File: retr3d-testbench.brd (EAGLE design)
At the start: 101.9 x 53.3 mm, 72 parts, among them U1 ARDUINO-MEGAFULL

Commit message: Update
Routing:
- net N$1: track 18.6 -> 20.7 mm
- net N$38: track 21.6 -> 23.1 mm
- net N$30: track 18.6 -> 19.5 mm
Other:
- board text added: "For assembly and usage goto"
- board text added: "Github.com/masterperson40/Retr3d-Testbench"

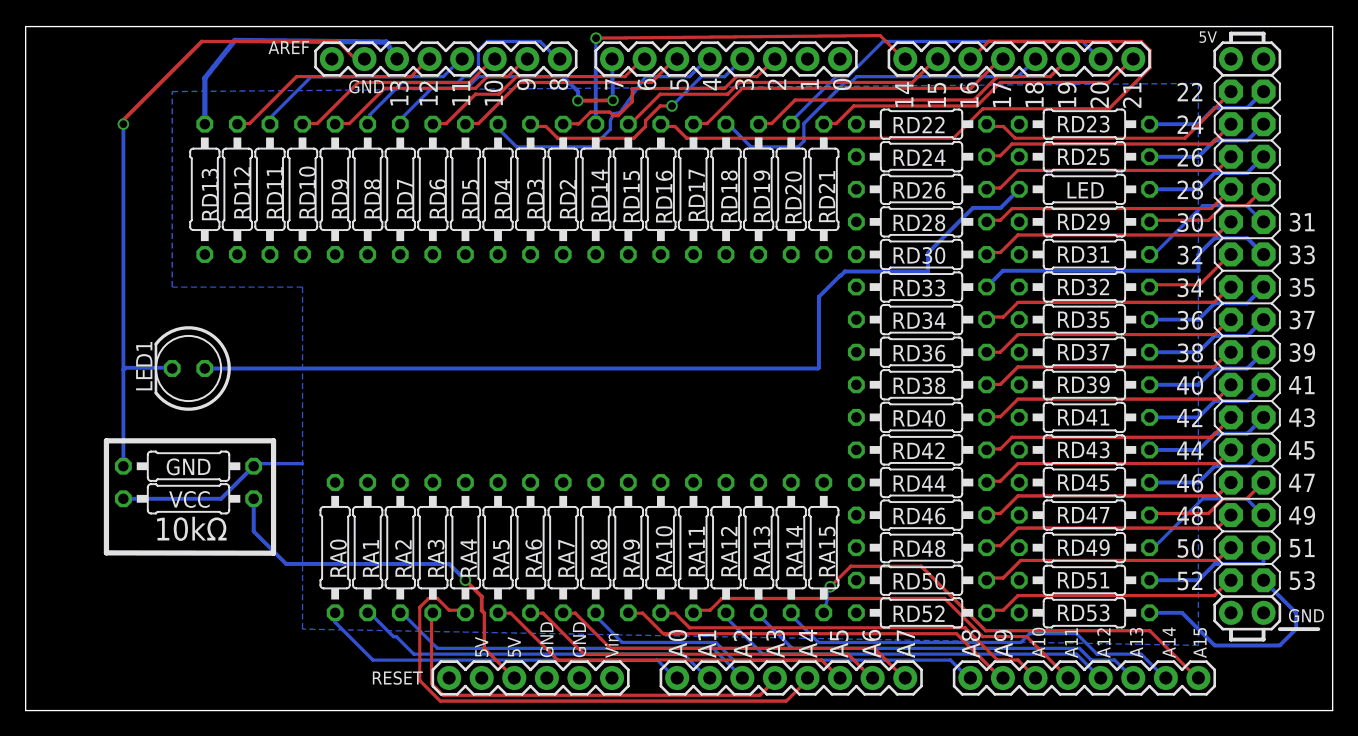
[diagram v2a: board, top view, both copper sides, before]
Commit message: Redesign for easier fabrication
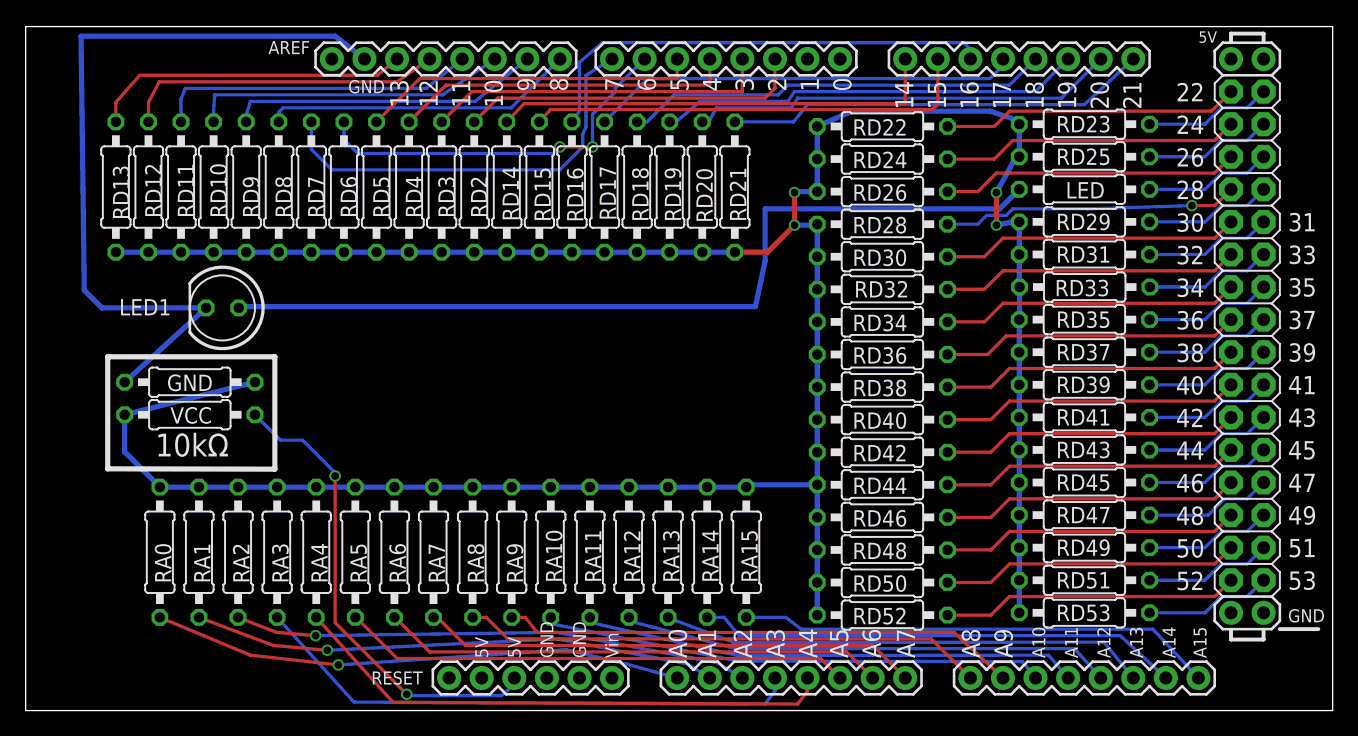
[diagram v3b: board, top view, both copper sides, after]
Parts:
- moved RD32 15.7 mm to (68.1, 50.6)
- moved RA0 13.7 mm to (11.7, 30.1)
- moved RA1 13.2 mm to (14.8, 30.1)
- moved RD33 12.7 mm to (83.8, 50.8)
- moved RA2 12.7 mm to (17.8, 30.1)
- moved RA3 12.1 mm to (20.9, 30.1)
- moved RA4 11.6 mm to (23.9, 30.1)
- moved RA5 11.1 mm to (27.0, 30.1)
- moved RA6 10.6 mm to (30.0, 30.1)
- moved RA7 10.1 mm to (33.1, 30.1)
- moved RA8 9.61 mm to (36.1, 30.1)
- moved RA9 9.10 mm to (39.2, 30.1)
- moved RA10 8.59 mm to (42.2, 30.1)
- moved RA11 8.09 mm to (45.3, 30.1)
- moved RA12 7.58 mm to (48.3, 30.1)
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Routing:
- net N$TEST: track 15.1 -> 221.3 mm, vias 0 -> 4
- net N$50: track 57.1 -> 36.8 mm
- net N$58: track 7.47 -> 23.2 mm
- net N$74: track 24.4 -> 9.92 mm
- net N$4: track 29.2 -> 41.3 mm, vias 0 -> 1
- net N$168: track 28.8 -> 40.8 mm, vias 0 -> 1
- net N$36: track 18.6 -> 30.0 mm, vias 0 -> 2
- net N$8: track 28.8 -> 40.1 mm, vias 0 -> 1
- net N$180: track 28.8 -> 39.8 mm
- net N$14: track 28.8 -> 39.2 mm
- net N$186: track 28.8 -> 38.7 mm
- net N$174: track 33.4 -> 43.3 mm
- net N$38: track 23.1 -> 32.7 mm, vias 2 -> 0
- net N$17: track 31.5 -> 40.8 mm
- net N$192: track 31.3 -> 40.3 mm
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- removed copper zone on layer 16, net N$TEST
